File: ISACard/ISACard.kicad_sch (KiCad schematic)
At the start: 78 parts, among them J1 Bus_ISA_8bit, J2 ICSP, J3 EXTSPI, J4 SERCON, J5 Conn_01x16, Q1 2N3904, SW1 SW_Push, U1 74LS86, U11 ATmega328P-P, U12 MicroSD_SPI_CD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

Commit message: Fixed some problems with the card...
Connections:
- net GND: no longer U4.12, U4.13
- net SEL8255: now also U4.11; no longer U3.11
- net AEN: now reaches J1.42 (AEN)
- net AEN: now also U4.13
- new net: U3.11, U4.12
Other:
- moved on the sheet: U4D

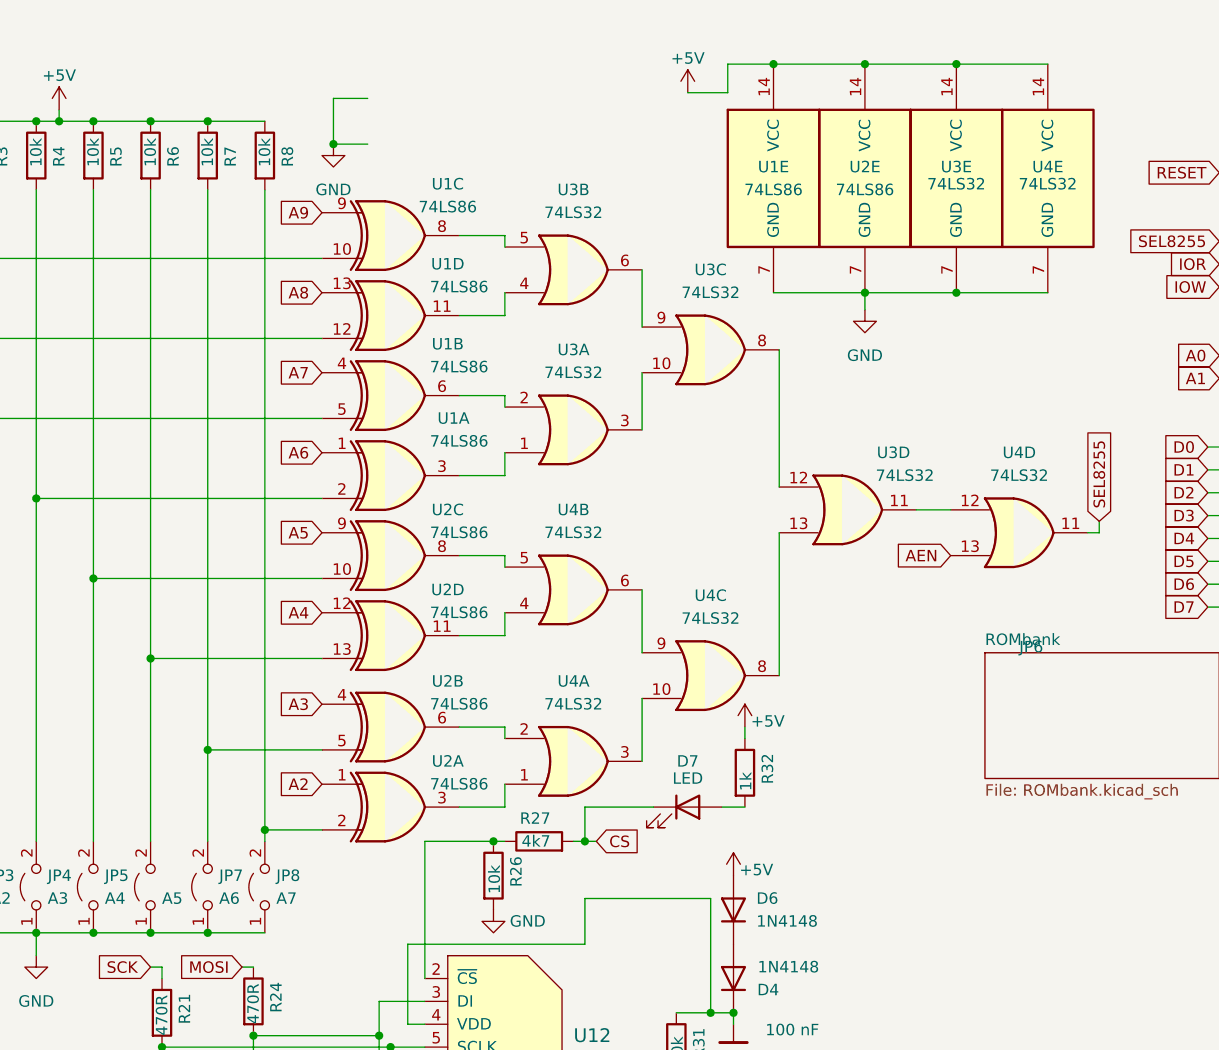
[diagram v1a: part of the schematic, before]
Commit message: fixed rom labels
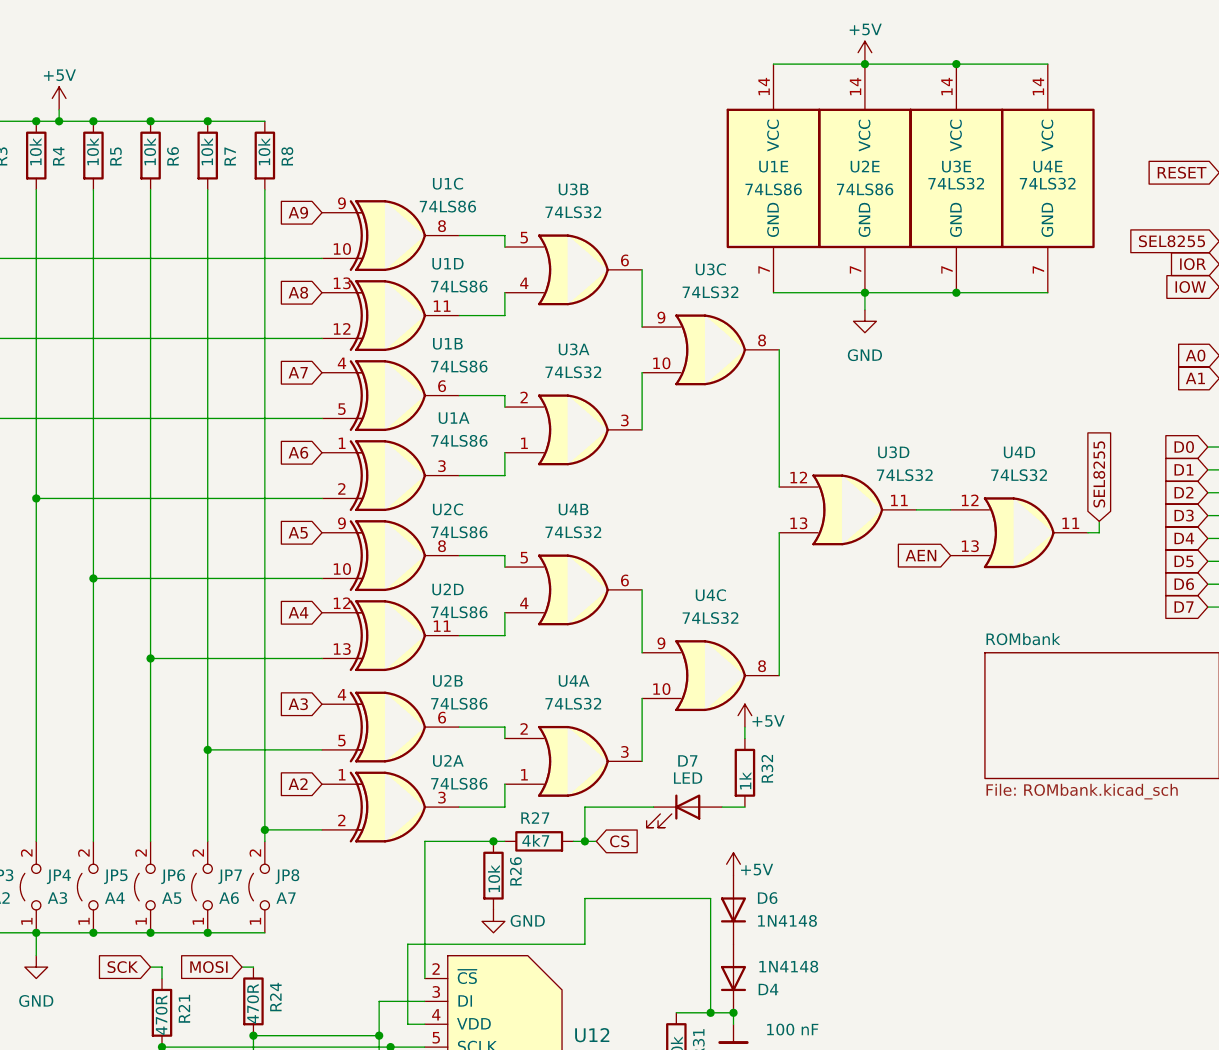
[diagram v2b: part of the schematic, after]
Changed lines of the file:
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@@
   (junction (at 199.39 153.67) (diameter 0) (color 0 0 0 0)
   )
-  (junction (at 140.97 29.21) (diameter 0) (color 0 0 0 0)
-  )
   (junction (at 127 96.52) (diameter 0) (color 0 0 0 0)
   )
@@
   (junction (at 21.59 124.46) (diameter 0) (color 0 0 0 0)
   )
-  (junction (at 189.865 20.32) (diameter 0) (color 0 0 0 0)
-  )
   (junction (at 200.025 45.72) (diameter 0) (color 0 0 0 0)
   )
@@
     (stroke (width 0) (type default))
   )
-  (wire (pts (xy 184.785 23.495) (xy 184.785 20.32))
-    (stroke (width 0) (type default))
-  )
   (wire (pts (xy 21.59 132.08) (xy 21.59 130.81))
     (stroke (width 0) (type default))
@@
     (stroke (width 0) (type default))
   )
-  (wire (pts (xy 140.97 24.13) (xy 144.78 24.13))
-    (stroke (width 0) (type default))
-  )
   (wire (pts (xy 73.66 81.28) (xy 77.47 81.28))
     (stroke (width 0) (type default))
@@
     (stroke (width 0) (type default))
   )
-  (wire (pts (xy 184.785 20.32) (xy 189.865 20.32))
-    (stroke (width 0) (type default))
-  )
   (wire (pts (xy 73.66 143.51) (xy 82.55 143.51))
     (stroke (width 0) (type default))
@@
     (stroke (width 0) (type default))
   )
-  (wire (pts (xy 140.97 29.21) (xy 140.97 24.13))
-    (stroke (width 0) (type default))
-  )
   (wire (pts (xy 267.97 124.46) (xy 271.78 124.46))
     (stroke (width 0) (type default))
@@
     (stroke (width 0) (type default))
   )
-  (wire (pts (xy 180.34 23.495) (xy 184.785 23.495))
-    (stroke (width 0) (type default))
-  )
   (wire (pts (xy 121.92 121.92) (xy 121.92 120.65))
     (stroke (width 0) (type default))
@@
     (stroke (width 0) (type default))
   )
-  (wire (pts (xy 140.97 29.21) (xy 144.78 29.21))
-    (stroke (width 0) (type default))
-  )
   (wire (pts (xy 21.59 124.46) (xy 26.67 124.46))
     (stroke (width 0) (type default))
@@
   (symbol (lib_id "Jumper:Jumper_2_Open") (at 120.65 111.76 90) (unit 1)
     (in_bom yes) (on_board yes) (dnp no)
-    (property "Reference" "JP6" (at 217.17 85.0899 90)
+    (property "Reference" "JP6" (at 121.92 110.49 90)
       (effects (font (size 1.27 1.27)) (justify right))
     )
@@
     )
   )
-  (symbol (lib_id "power:GND") (at 140.97 29.21 0) (unit 1)
-    (in_bom yes) (on_board yes) (dnp no) (fields_autoplaced)
-    (property "Reference" "#PWR0106" (at 140.97 35.56 0)
-      (effects (font (size 1.27 1.27)) hide)
-    )
-    (property "Value" "GND" (at 140.97 34.29 0)
-      (effects (font (size 1.27 1.27)))
-    )
-    (property "Footprint" "" (at 140.97 29.21 0)
-      (effects (font (size 1.27 1.27)) hide)
-    )
-    (property "Datasheet" "" (at 140.97 29.21 0)
-      (effects (font (size 1.27 1.27)) hide)
-    )
-    (pin "1")
-    (instances
-      (project "ISACard"
-        (path "/02f59ec8-9e35-4f4f-ad74-c5620a79c783"
-          (reference "#PWR0106") (unit 1)
-        )
-      )
-    )
-  )
   (symbol (lib_id "Device:R") (at 105.41 161.29 0) (unit 1)
     (in_bom yes) (on_board yes) (dnp no)
@@
     )
   )
-  (symbol (lib_id "power:+5V") (at 180.34 23.495 0) (unit 1)
+  (symbol (lib_id "power:+5V") (at 200.025 20.32 0) (unit 1)
     (in_bom yes) (on_board yes) (dnp no)
-    (property "Reference" "#PWR0109" (at 180.34 27.305 0)
+    (property "Reference" "#PWR0109" (at 200.025 24.13 0)
       (effects (font (size 1.27 1.27)) hide)
     )
-    (property "Value" "+5V" (at 180.34 19.685 0)
+    (property "Value" "+5V" (at 200.025 16.51 0)
       (effects (font (size 1.27 1.27)))
     )
-    (property "Footprint" "" (at 180.34 23.495 0)
+    (property "Footprint" "" (at 200.025 20.32 0)
       (effects (font (size 1.27 1.27)) hide)
     )
-    (property "Datasheet" "" (at 180.34 23.495 0)
+    (property "Datasheet" "" (at 200.025 20.32 0)
       (effects (font (size 1.27 1.27)) hide)
     )

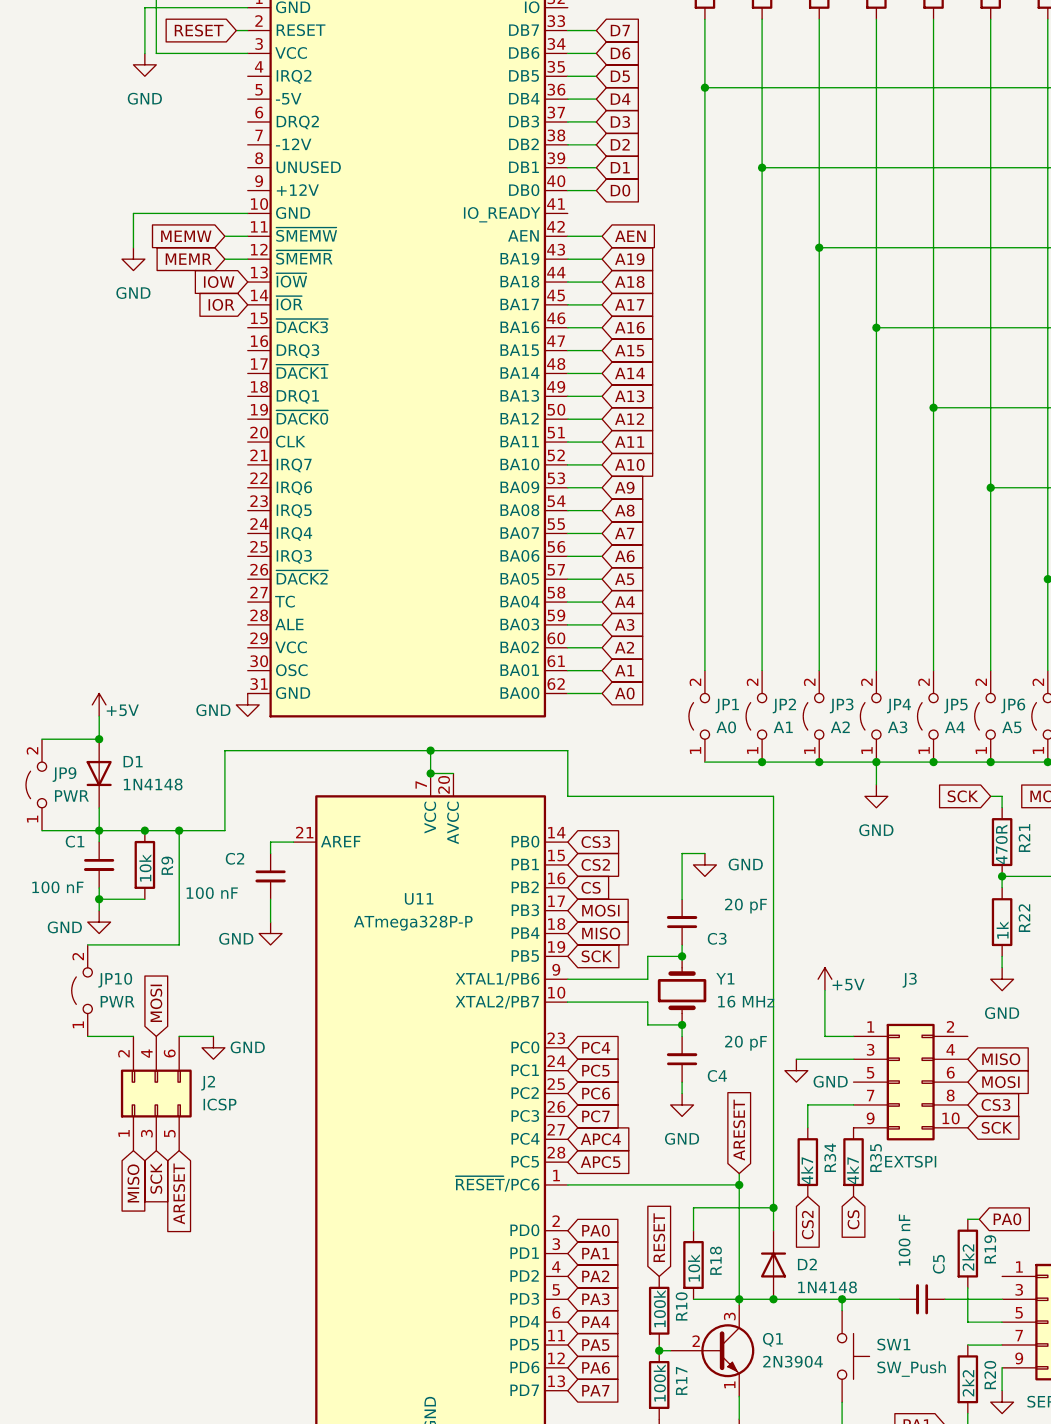
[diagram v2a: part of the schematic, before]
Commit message: Added IRQ connection to ethernet
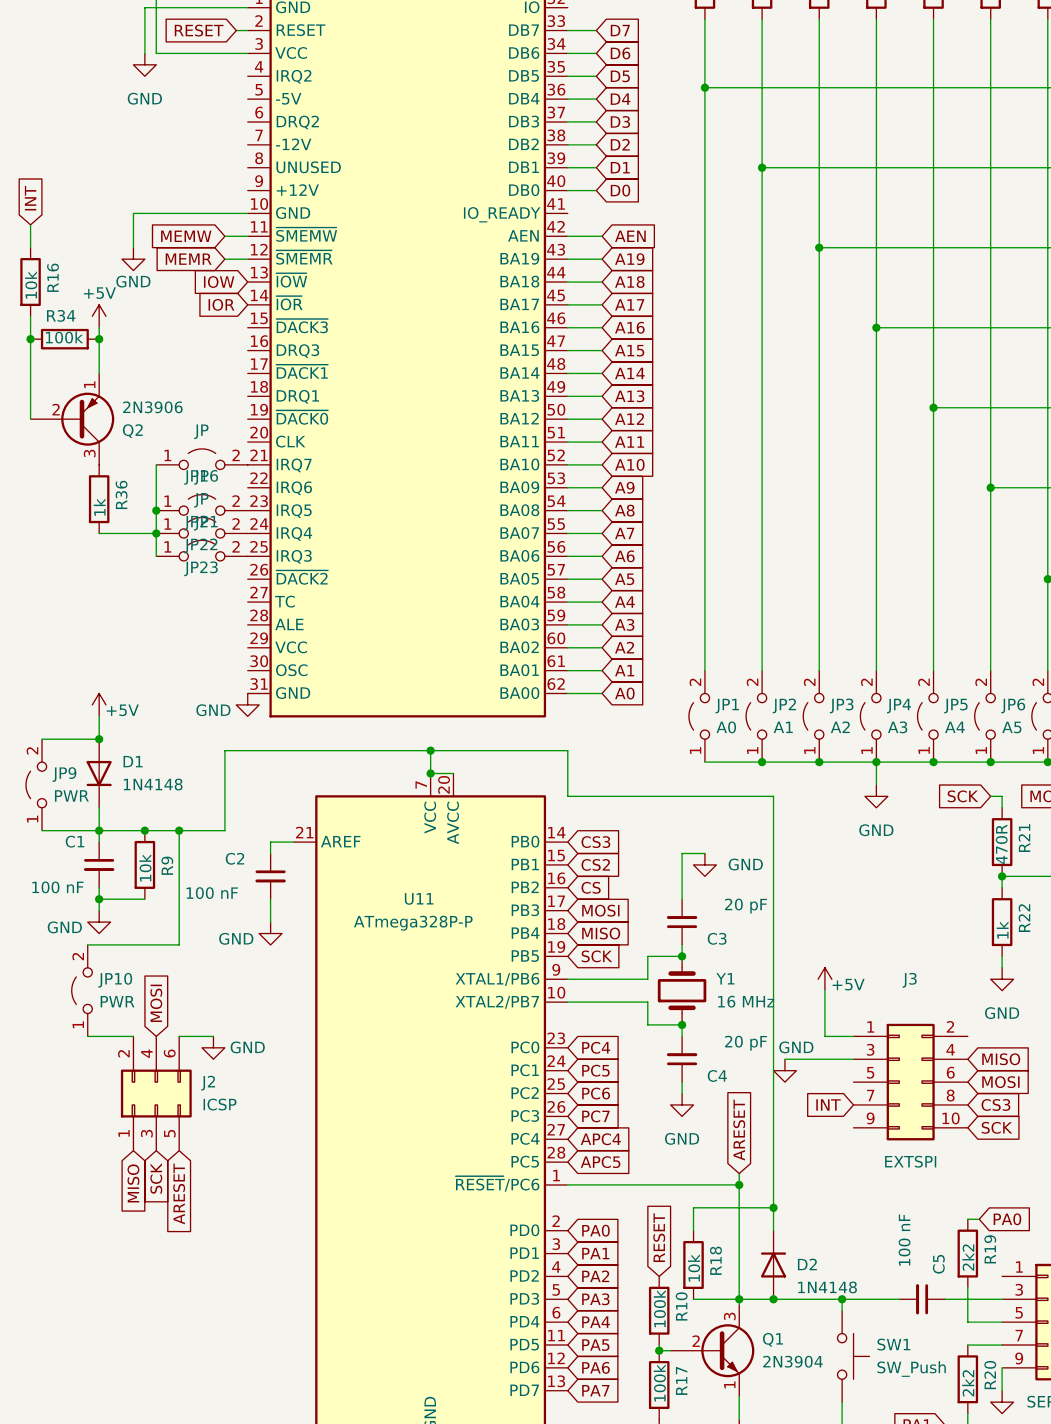
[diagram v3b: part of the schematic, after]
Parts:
- removed R35: 4k7, Resistor_THT:R_Axial_DIN0207_L6.3mm_D2.5mm_P7.62mm_Horizontal, symbol Device:R
- added JP16, JP21, JP22, JP23: JP, Connector_PinHeader_2.54mm:PinHeader_1x02_P2.54mm_Vertical, symbol Jumper:Jumper_2_Open
- added Q2: 2N3906, Package_TO_SOT_THT:TO-92_Inline_Wide, symbol Transistor_BJT:2N3906
- added R16: 10k, Resistor_THT:R_Axial_DIN0207_L6.3mm_D2.5mm_P7.62mm_Horizontal, symbol Device:R
- added R36: 1k, Resistor_THT:R_Axial_DIN0207_L6.3mm_D2.5mm_P7.62mm_Horizontal, symbol Device:R
- R34: value 4k7 -> 100k
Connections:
- net +5V: now also R34.2, Q2.1 (E)
- net CS2: no longer R34.2
- net at R34.1: now also Q2.2 (B), R16.2; no longer J3.7 (Pin_7)
- net at J1.21 (IRQ7): now also JP16.2 (B)
- net at J1.23 (IRQ5): now also JP21.2 (B)
- net at J1.24 (IRQ4): now also JP22.2 (B)
- net at J1.25 (IRQ3): now also JP23.2 (B)
- new net: Q2.3 (C), R36.1
- new net: JP16.1 (A), JP21.1 (A), JP22.1 (A), JP23.1 (A), R36.2
- new net INT: J3.7 (Pin_7), R16.1

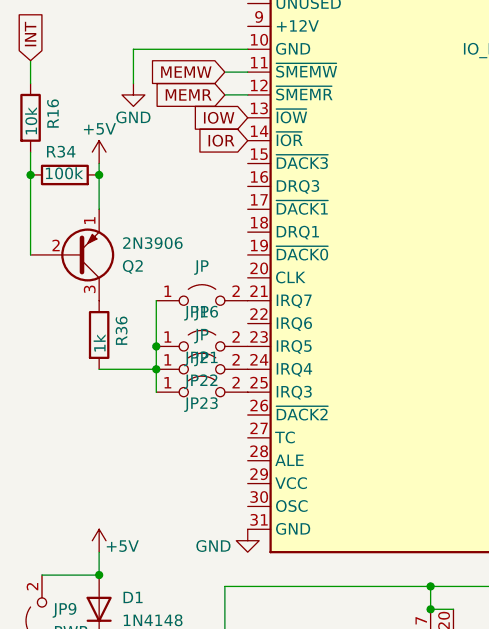
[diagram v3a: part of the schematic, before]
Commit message: Adjusted bias of resistors
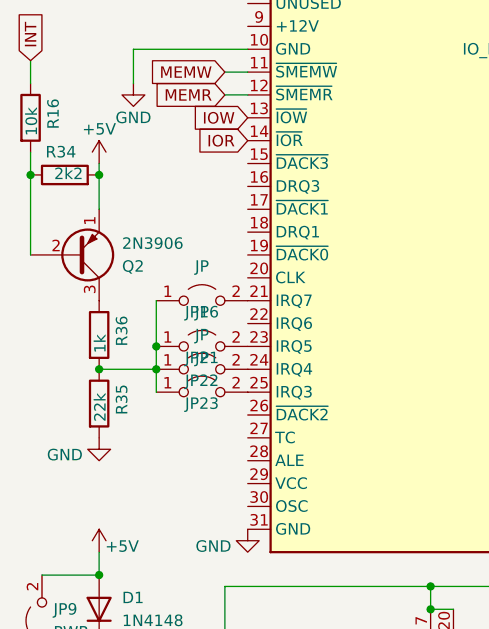
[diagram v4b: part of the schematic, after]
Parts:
- added R35: 22k, Resistor_THT:R_Axial_DIN0207_L6.3mm_D2.5mm_P7.62mm_Horizontal, symbol Device:R
- R34: value 100k -> 2k2
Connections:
- net GND: now also R35.2
- net at JP16.1 (A), JP21.1 (A), JP22.1 (A)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: now also R35.1
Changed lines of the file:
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@@
   (junction (at 210.185 45.72) (diameter 0) (color 0 0 0 0)
   )
+  (junction (at 21.59 91.44) (diameter 0) (color 0 0 0 0)
+  )
   (junction (at 104.14 176.53) (diameter 0) (color 0 0 0 0)
   )
@@
     )
   )
+  (symbol (lib_id "Device:R") (at 21.59 95.25 0) (unit 1)
+    (in_bom yes) (on_board yes) (dnp no)
+    (property "Reference" "R35" (at 24.13 96.52 90)
+      (effects (font (size 1.27 1.27)) (justify left))
+    )
+    (property "Value" "22k" (at 21.717 97.282 90)
+      (effects (font (size 1.27 1.27)) (justify left))
+    )
+    (property "Footprint" "Resistor_THT:R_Axial_DIN0207_L6.3mm_D2.5mm_P7.62mm_Horizontal" (at 19.812 95.25 90)
+      (effects (font (size 1.27 1.27)) hide)
+    )
+    (property "Datasheet" "~" (at 21.59 95.25 0)
+      (effects (font (size 1.27 1.27)) hide)
+    )
+    (pin "1")
+    (pin "2")
+    (instances
+      (project "ISACard"
+        (path "/02f59ec8-9e35-4f4f-ad74-c5620a79c783"
+          (reference "R35") (unit 1)
+        )
+      )
+    )
+  )
   (symbol (lib_id "power:+5V") (at 110.49 25.4 0) (unit 1)
     (in_bom yes) (on_board yes) (dnp no)
@@
     )
   )
+  (symbol (lib_id "power:GND") (at 21.59 99.06 0) (unit 1)
+    (in_bom yes) (on_board yes) (dnp no)
+    (property "Reference" "#PWR04" (at 21.59 105.41 0)
+      (effects (font (size 1.27 1.27)) hide)
+    )
+    (property "Value" "GND" (at 17.78 100.965 0)
+      (effects (font (size 1.27 1.27)))
+    )
+    (property "Footprint" "" (at 21.59 99.06 0)
+      (effects (font (size 1.27 1.27)) hide)
+    )
+    (property "Datasheet" "" (at 21.59 99.06 0)
+      (effects (font (size 1.27 1.27)) hide)
+    )
+    (pin "1")
+    (instances
+      (project "ISACard"
+        (path "/02f59ec8-9e35-4f4f-ad74-c5620a79c783"
+          (reference "#PWR04") (unit 1)
+        )
+      )
+    )
+  )
   (symbol (lib_id "Jumper:Jumper_2_Open") (at 127 111.76 90) (unit 1)
     (in_bom yes) (on_board yes) (dnp no) (fields_autoplaced)
@@
       (effects (font (size 1.27 1.27)) (justify left))
     )
-    (property "Value" "100k" (at 19.812 69.723 90)
+    (property "Value" "2k2" (at 19.812 69.723 90)
       (effects (font (size 1.27 1.27)) (justify left))
     )
